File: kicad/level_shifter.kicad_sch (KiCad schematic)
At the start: 32 parts, among them U3 74LVC2T45GT, U4 74LVC2T45GT, U5 74LVC2T45GT, U6 74LVC2T45GT

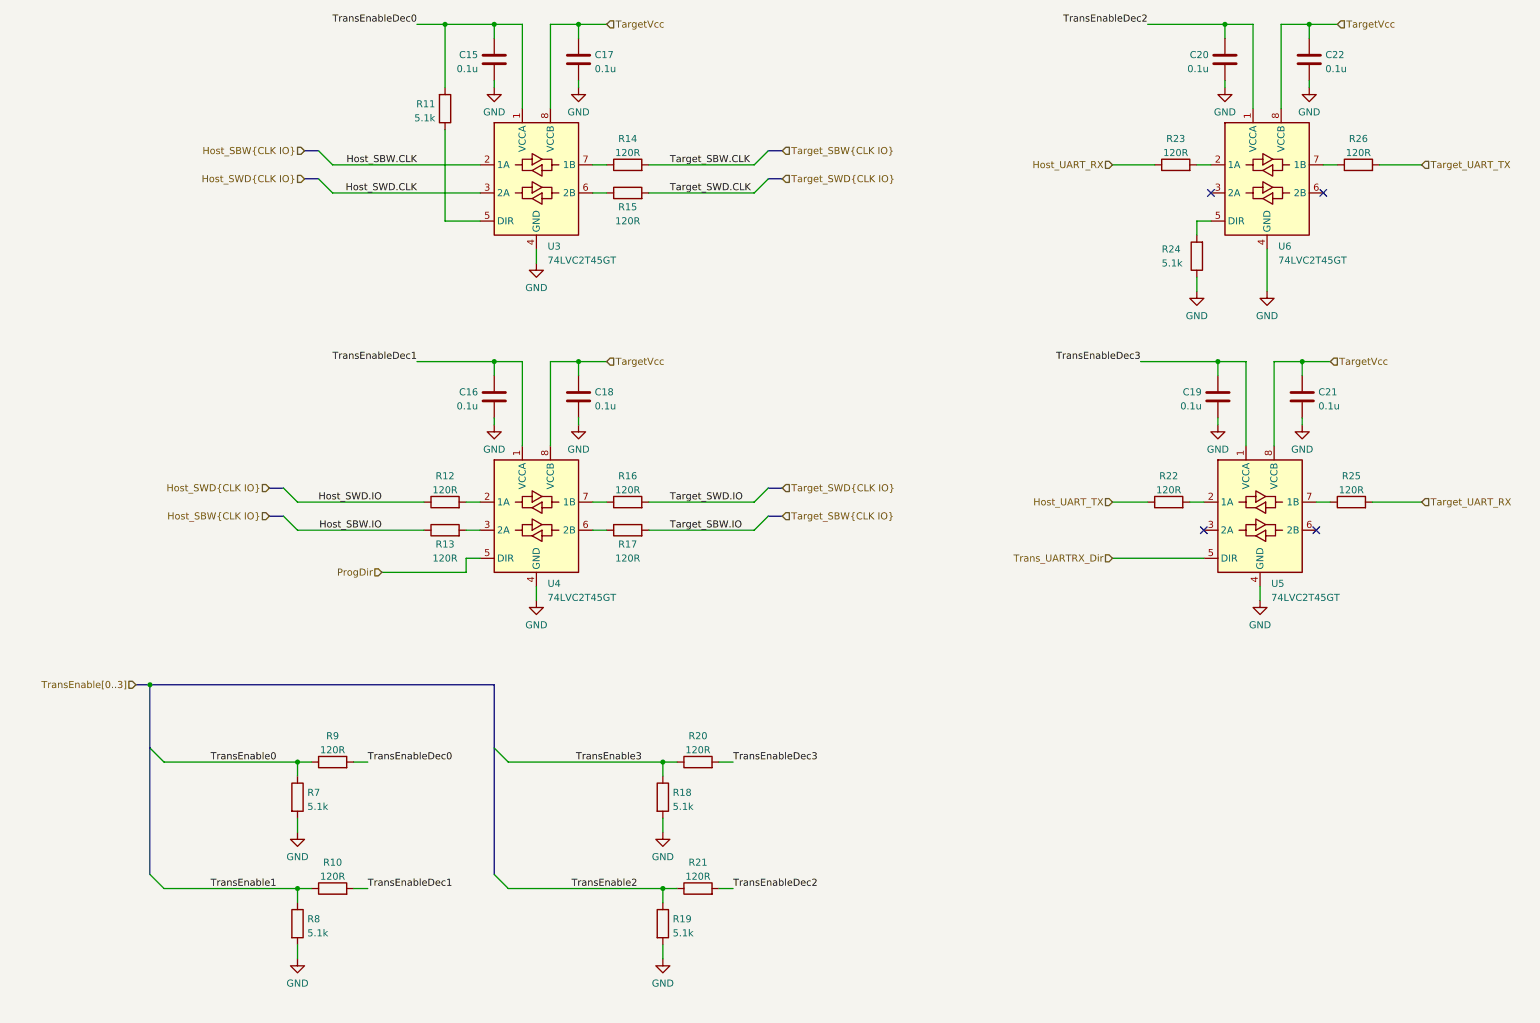
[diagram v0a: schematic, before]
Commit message: add fourth level converter for simultaneous programming + TX/RX
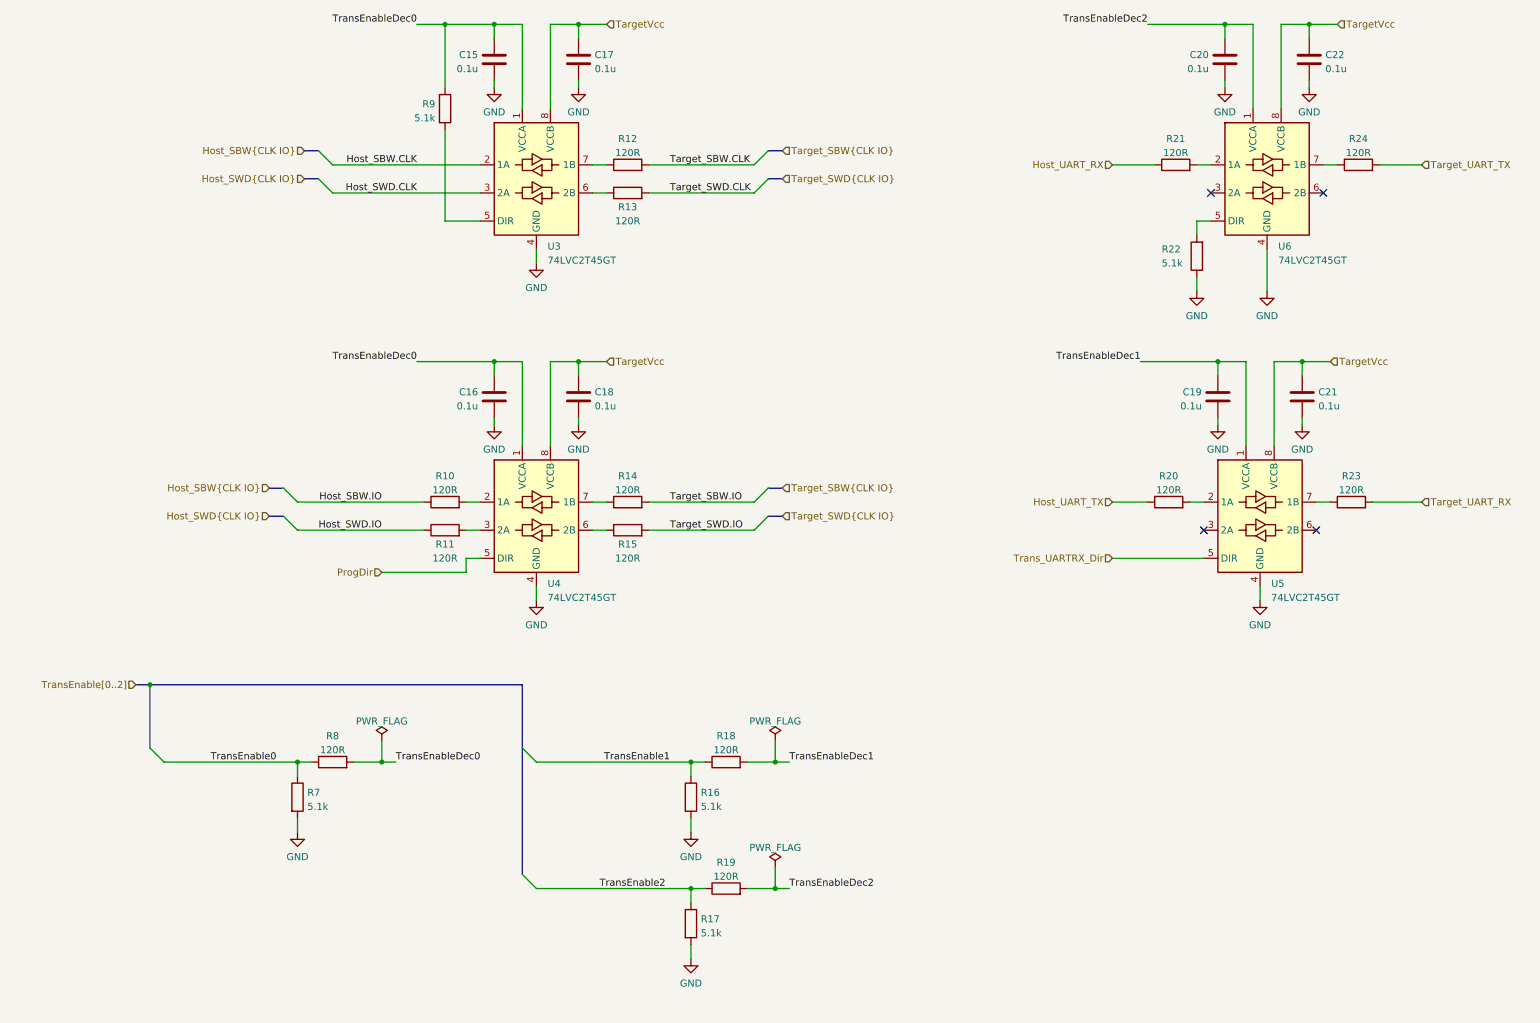
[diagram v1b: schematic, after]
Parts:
- removed R10: 120R, Resistor_SMD:R_0402_1005Metric, symbol Device:R
- removed R8: 5.1k, Resistor_SMD:R_0402_1005Metric, symbol Device:R
- renumbered C19 to C16, C21 to C18, C20 to C19, C16 to C20, C22 to C21, C18 to C22, R22 to R10, R13 to R11, R14 to R12, R15 to R13, R16 to R14, R17 to R15, R19 to R16, R18 to R17, R21 to R18, R20 to R19, R23 to R20, R12 to R21, R24 to R22, R26 to R23, R25 to R24, R9 to R8, R11 to R9, U5 to U4, U6 to U5, U4 to U6
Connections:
- net TransEnable3 is gone; now on net TransEnable2: R17.1, R19.1
- net Host_SBW.IO: now also R10.1; no longer R11.1
- net Host_SWD.IO: now also R11.1; no longer R21.1
- net Host_UART_RX: now also R21.1; no longer R20.1
- net Host_UART_TX: now also R20.1; no longer R10.1
- net ProgDir: now also U4.5 (DIR); no longer U6.5 (DIR)
- net Target_SBW.IO: now also R14.2; no longer R15.2
- net Target_SWD.IO: now also R15.2; no longer R14.2
- net Target_UART_RX: now also R23.2; no longer R24.2
- net Target_UART_TX: now also R24.2; no longer R23.2
- net TransEnable1: now also R16.1, R18.1
- net TransEnable2: no longer R16.1, R18.1
- net TransEnableDec0: now also C16.2, U4.1 (VCCA)
- net TransEnableDec1: now also C19.2, R18.2, U5.1 (VCCA); no longer C20.2, U6.1 (VCCA)
- net TransEnableDec2: now also C20.2, R19.2, U6.1 (VCCA); no longer C19.2, R18.2, U5.1 (VCCA)
- net Trans_UARTRX_Dir: now also U5.5 (DIR); no longer U4.5 (DIR)
- net at R22.2: now also U6.5 (DIR); no longer U5.5 (DIR)
- net at R11.2: now also U4.3 (2A); no longer U6.3 (2A)
- net at U6.6 (2B): no longer R15.1
- net at U6.7 (1B): now also R24.1; no longer R14.1
- net at U4.6 (2B): now also R15.1
- net at U4.7 (1B): now also R14.1; no longer R24.1
- removed net TransEnableDec3: C16.2, R19.2, U4.1 (VCCA)
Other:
- moved on the sheet: C16, C18, C19, C20, C21, C22, R10, R16, R17, R18, R19, R20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

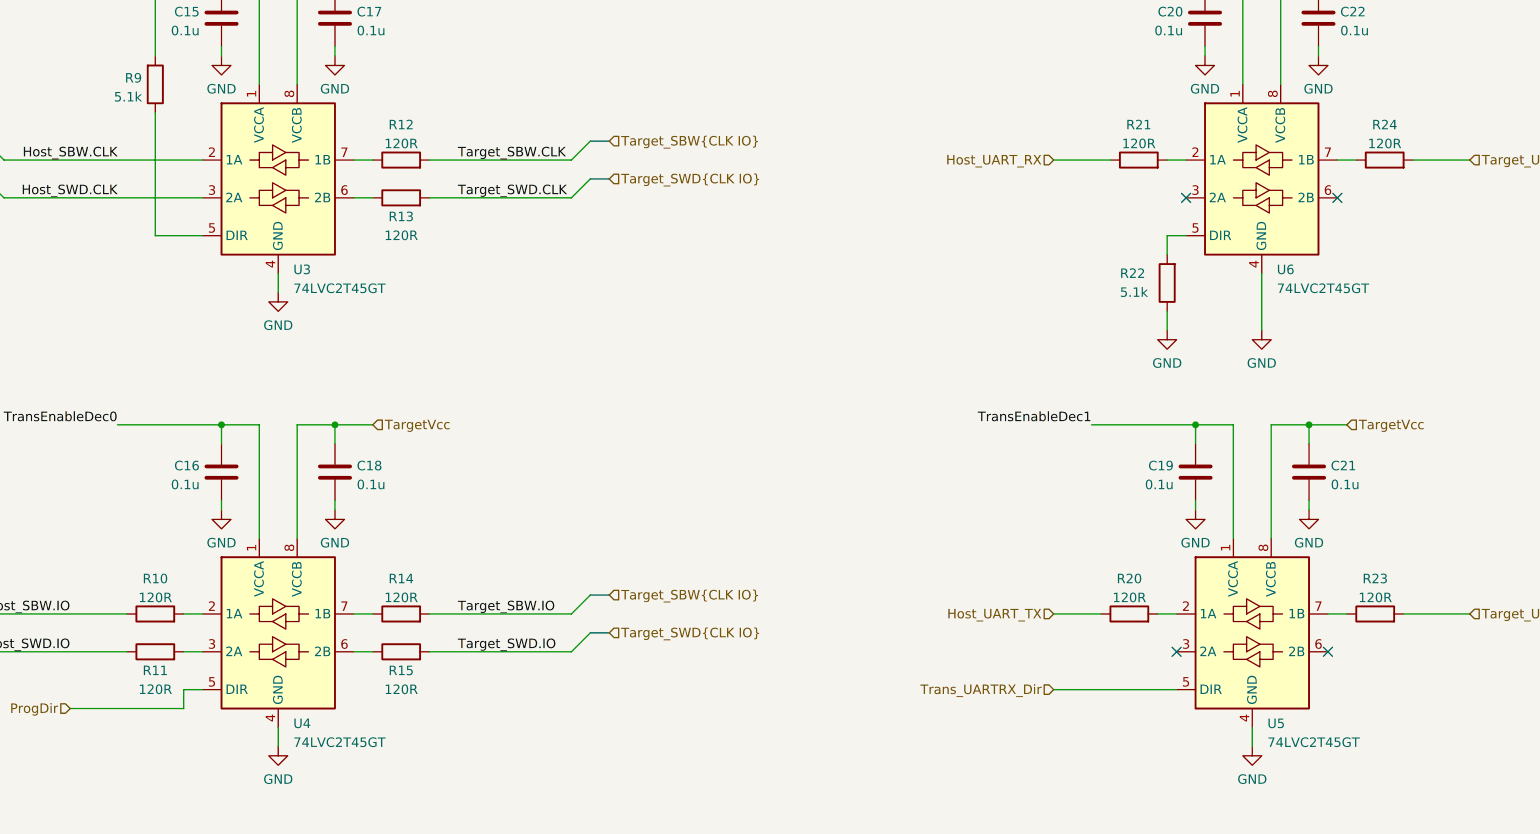
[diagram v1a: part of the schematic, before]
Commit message: adjust values of level translator series resistors
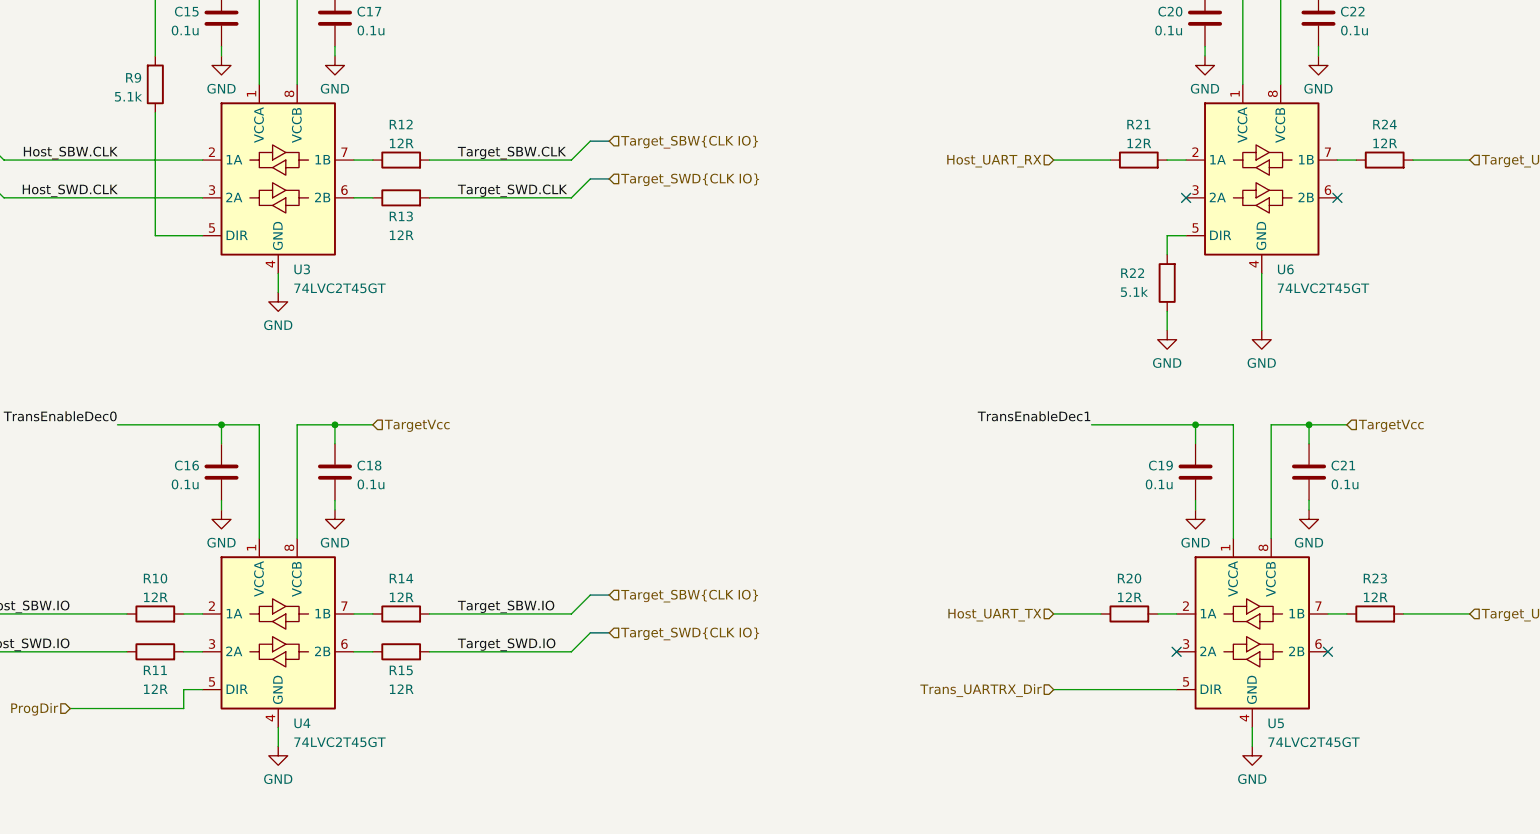
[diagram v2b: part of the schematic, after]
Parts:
- R10, R11, R12, R13, R14, R15, R20, R21, R23, R24: value 120R -> 12R
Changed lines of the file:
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@@
     (pin "1")
   )
-  (symbol (lib_name "74LVC2T45GT_3") (lib_id "riotee:74LVC2T45GT") (at 236.22 106.68 0) (unit 1)
+  (symbol (lib_id "riotee:74LVC2T45GT") (at 236.22 106.68 0) (unit 1)
     (in_bom yes) (on_board yes) (fields_autoplaced)
     (property "Reference" "U5" (id 0) (at 238.2394 118.8704 0)
@@
       (effects (font (size 1.27 1.27)) (justify left))
     )
-    (property "Footprint" "riotee:NXP_SOT833-1" (id 2) (at 236.22 128.27 0)
+    (property "Footprint" "riotee:NXP_SOT833-1" (id 2) (at 236.22 129.54 0)
       (effects (font (size 1.27 1.27)) hide)
     )
@@
     (pin "1")
   )
-  (symbol (lib_name "74LVC2T45GT_1") (lib_id "riotee:74LVC2T45GT") (at 105.41 45.72 0) (unit 1)
+  (symbol (lib_id "riotee:74LVC2T45GT") (at 105.41 45.72 0) (unit 1)
     (in_bom yes) (on_board yes) (fields_autoplaced)
     (property "Reference" "U3" (id 0) (at 107.4294 57.9104 0)
@@
       (effects (font (size 1.27 1.27)) (justify left))
     )
-    (property "Footprint" "riotee:NXP_SOT833-1" (id 2) (at 105.41 67.31 0)
+    (property "Footprint" "riotee:NXP_SOT833-1" (id 2) (at 105.41 68.58 0)
       (effects (font (size 1.27 1.27)) hide)
     )
@@
     (in_bom yes) (on_board yes) (fields_autoplaced)
     (property "Reference" "R21" (id 0) (at 220.98 38.4642 90))
-    (property "Value" "120R" (id 1) (at 220.98 41.0011 90))
+    (property "Value" "12R" (id 1) (at 220.98 41.0011 90))
     (property "Footprint" "Resistor_SMD:R_0402_1005Metric" (id 2) (at 220.98 44.958 90)
       (effects (font (size 1.27 1.27)) hide)
@@
     (in_bom yes) (on_board yes) (fields_autoplaced)
     (property "Reference" "R23" (id 0) (at 252.73 99.4242 90))
-    (property "Value" "120R" (id 1) (at 252.73 101.9611 90))
+    (property "Value" "12R" (id 1) (at 252.73 101.9611 90))
     (property "Footprint" "Resistor_SMD:R_0402_1005Metric" (id 2) (at 252.73 105.918 90)
       (effects (font (size 1.27 1.27)) hide)
@@
     (in_bom yes) (on_board yes)
     (property "Reference" "R13" (id 0) (at 121.92 50.8 90))
-    (property "Value" "120R" (id 1) (at 121.92 53.3369 90))
+    (property "Value" "12R" (id 1) (at 121.92 53.3369 90))
     (property "Footprint" "Resistor_SMD:R_0402_1005Metric" (id 2) (at 121.92 50.038 90)
       (effects (font (size 1.27 1.27)) hide)
@@
     (in_bom yes) (on_board yes)
     (property "Reference" "R11" (id 0) (at 88.9 111.76 90))
-    (property "Value" "120R" (id 1) (at 88.9 114.2969 90))
+    (property "Value" "12R" (id 1) (at 88.9 114.2969 90))
     (property "Footprint" "Resistor_SMD:R_0402_1005Metric" (id 2) (at 88.9 110.998 90)
       (effects (font (size 1.27 1.27)) hide)
@@
     (in_bom yes) (on_board yes) (fields_autoplaced)
     (property "Reference" "R10" (id 0) (at 88.9 99.4242 90))
-    (property "Value" "120R" (id 1) (at 88.9 101.9611 90))
+    (property "Value" "12R" (id 1) (at 88.9 101.9611 90))
     (property "Footprint" "Resistor_SMD:R_0402_1005Metric" (id 2) (at 88.9 105.918 90)
       (effects (font (size 1.27 1.27)) hide)
@@
     (in_bom yes) (on_board yes) (fields_autoplaced)
     (property "Reference" "R12" (id 0) (at 121.92 38.4642 90))
-    (property "Value" "120R" (id 1) (at 121.92 41.0011 90))
+    (property "Value" "12R" (id 1) (at 121.92 41.0011 90))
     (property "Footprint" "Resistor_SMD:R_0402_1005Metric" (id 2) (at 121.92 44.958 90)
       (effects (font (size 1.27 1.27)) hide)
@@
       (effects (font (size 1.27 1.27)) (justify left))
     )
-    (property "Footprint" "riotee:NXP_SOT833-1" (id 2) (at 237.49 67.31 0)
+    (property "Footprint" "riotee:NXP_SOT833-1" (id 2) (at 237.49 68.58 0)
       (effects (font (size 1.27 1.27)) hide)
     )
@@
     (in_bom yes) (on_board yes) (fields_autoplaced)
     (property "Reference" "R14" (id 0) (at 121.92 99.4242 90))
-    (property "Value" "120R" (id 1) (at 121.92 101.9611 90))
+    (property "Value" "12R" (id 1) (at 121.92 101.9611 90))
     (property "Footprint" "Resistor_SMD:R_0402_1005Metric" (id 2) (at 121.92 105.918 90)
       (effects (font (size 1.27 1.27)) hide)
@@
     (in_bom yes) (on_board yes)
     (property "Reference" "R15" (id 0) (at 121.92 111.7631 90))
-    (property "Value" "120R" (id 1) (at 121.92 114.3 90))
+    (property "Value" "12R" (id 1) (at 121.92 114.3 90))
     (property "Footprint" "Resistor_SMD:R_0402_1005Metric" (id 2) (at 121.92 110.998 90)
       (effects (font (size 1.27 1.27)) hide)
@@
     (in_bom yes) (on_board yes) (fields_autoplaced)
     (property "Reference" "R20" (id 0) (at 219.71 99.4242 90))
-    (property "Value" "120R" (id 1) (at 219.71 101.9611 90))
+    (property "Value" "12R" (id 1) (at 219.71 101.9611 90))
     (property "Footprint" "Resistor_SMD:R_0402_1005Metric" (id 2) (at 219.71 105.918 90)
       (effects (font (size 1.27 1.27)) hide)
@@
     (pin "1")
   )
-  (symbol (lib_name "74LVC2T45GT_2") (lib_id "riotee:74LVC2T45GT") (at 105.41 106.68 0) (unit 1)
+  (symbol (lib_id "riotee:74LVC2T45GT") (at 105.41 106.68 0) (unit 1)
     (in_bom yes) (on_board yes) (fields_autoplaced)
     (property "Reference" "U4" (id 0) (at 107.4294 118.8704 0)
@@
       (effects (font (size 1.27 1.27)) (justify left))
     )
-    (property "Footprint" "riotee:NXP_SOT833-1" (id 2) (at 105.41 128.27 0)
+    (property "Footprint" "riotee:NXP_SOT833-1" (id 2) (at 105.41 129.54 0)
       (effects (font (size 1.27 1.27)) hide)
     )
@@
     (in_bom yes) (on_board yes) (fields_autoplaced)
     (property "Reference" "R24" (id 0) (at 254 38.4642 90))
-    (property "Value" "120R" (id 1) (at 254 41.0011 90))
+    (property "Value" "12R" (id 1) (at 254 41.0011 90))
     (property "Footprint" "Resistor_SMD:R_0402_1005Metric" (id 2) (at 254 44.958 90)
       (effects (font (size 1.27 1.27)) hide)
